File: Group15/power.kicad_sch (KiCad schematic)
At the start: 4 parts, among them J1 USB_C_Receptacle_USB2.0_16P, U3 AP63205WU

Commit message: corrected Power
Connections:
- net GND: no longer J1.A4 (VBUS), J1.A6 (D+), J1.A7 (D-), J1.A9 (VBUS), J1.B4 (VBUS), J1.B6 (D+), J1.B7 (D-), J1.B9 (VBUS)
- new net USB_D+: J1.A6 (D+), J1.B6 (D+)
- new net USB_D-: J1.A7 (D-), J1.B7 (D-)
- new net VBUS: J1.A4 (VBUS), J1.A9 (VBUS), J1.B4 (VBUS), J1.B9 (VBUS)
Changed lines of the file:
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@@
 	(paper "A4")
 	(junction
-		(at 67.31 113.03)
-		(diameter 0)
-		(color 0 0 0 0)
-	)
-	(junction
 		(at 59.69 85.09)
 		(diameter 0)
@@
 	)
 	(junction
-		(at 74.93 85.09)
-		(diameter 0)
-		(color 0 0 0 0)
-	)
-	(junction
-		(at 67.31 90.17)
-		(diameter 0)
-		(color 0 0 0 0)
-	)
-	(junction
 		(at 39.37 113.03)
 		(diameter 0)
@@
 	)
 	(junction
-		(at 55.88 113.03)
-		(diameter 0)
-		(color 0 0 0 0)
-	)
-	(junction
 		(at 63.5 71.12)
 		(diameter 0)
@@
 	)
 	(junction
-		(at 74.93 113.03)
-		(diameter 0)
-		(color 0 0 0 0)
-	)
-	(junction
 		(at 46.99 113.03)
 		(diameter 0)
@@
 	(junction
 		(at 59.69 90.17)
-		(diameter 0)
-		(color 0 0 0 0)
-	)
-	(junction
-		(at 88.9 71.12)
 		(diameter 0)
 		(color 0 0 0 0)
@@
 	(wire
 		(pts
-			(xy 63.5 71.12) (xy 88.9 71.12)
-		)
-		(stroke
-			(width 0)
-			(type default)
-		)
-	)
-	(wire
-		(pts
 			(xy 46.99 113.03) (xy 39.37 113.03)
 		)
@@
 	(wire
 		(pts
-			(xy 74.93 85.09) (xy 91.44 85.09)
-		)
-		(stroke
-			(width 0)
-			(type default)
-		)
-	)
-	(wire
-		(pts
-			(xy 88.9 71.12) (xy 91.44 71.12)
+			(xy 59.69 85.09) (xy 91.44 85.09)
+		)
+		(stroke
+			(width 0)
+			(type default)
+		)
+	)
+	(wire
+		(pts
+			(xy 63.5 71.12) (xy 91.44 71.12)
 		)
 		(stroke
@@
 	(wire
 		(pts
-			(xy 67.31 113.03) (xy 67.31 90.17)
-		)
-		(stroke
-			(width 0)
-			(type default)
-		)
-	)
-	(wire
-		(pts
 			(xy 59.69 83.82) (xy 59.69 85.09)
 		)
@@
 	(wire
 		(pts
-			(xy 74.93 113.03) (xy 74.93 85.09)
-		)
-		(stroke
-			(width 0)
-			(type default)
-		)
-	)
-	(wire
-		(pts
 			(xy 59.69 86.36) (xy 54.61 86.36)
 		)
@@
 	(wire
 		(pts
-			(xy 91.44 90.17) (xy 67.31 90.17)
-		)
-		(stroke
-			(width 0)
-			(type default)
-		)
-	)
-	(wire
-		(pts
 			(xy 59.69 88.9) (xy 59.69 90.17)
 		)
@@
 	(wire
 		(pts
-			(xy 67.31 90.17) (xy 59.69 90.17)
+			(xy 59.69 90.17) (xy 91.44 90.17)
 		)
 		(stroke
@@
 		)
 		(stroke
-			(width 0)
-			(type default)
-		)
-	)
-	(wire
-		(pts
-			(xy 59.69 85.09) (xy 74.93 85.09)
-		)
-		(stroke
-			(width 0)
-			(type default)
-		)
-	)
-	(wire
-		(pts
-			(xy 55.88 113.03) (xy 88.9 113.03)
-		)
-		(stroke
-			(width 0)
-			(type default)
-		)
-	)
-	(wire
-		(pts
-			(xy 88.9 113.03) (xy 88.9 71.12)
-		)
-		(stroke

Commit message: ADC
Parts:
- added C4, C5: 100 nF, symbol Device:C_Small
- added C6: 10 uF, symbol Device:C_Small
- added DAC1: (no value), symbol Symbol_Library:MCP4716A0T-E/CH
- added R8, R9: 5k6, symbol Device:R
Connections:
- net GND: now also C4.2, C5.2, C6.2, DAC1.2 (Vss)
- new net: DAC1.4 (SDA), R9.2
- new net: DAC1.5 (SCL), R8.2
- new net +3.3V: C4.1, C6.1, DAC1.3 (VDD), R8.1, R9.1
- new net DAC_OUT: C5.1, DAC1.1 (Vout)
- no-connect marks 2 -> 3

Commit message: added Footprint for DAC
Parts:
- DAC1: footprint (none) -> Package_TO_SOT_SMD:SOT-23-6
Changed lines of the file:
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@@
 			)
 		)
-		(property "Footprint" ""
+		(property "Footprint" "Package_TO_SOT_SMD:SOT-23-6"
 			(at 212.09 87.63 0)
 			(hide yes)

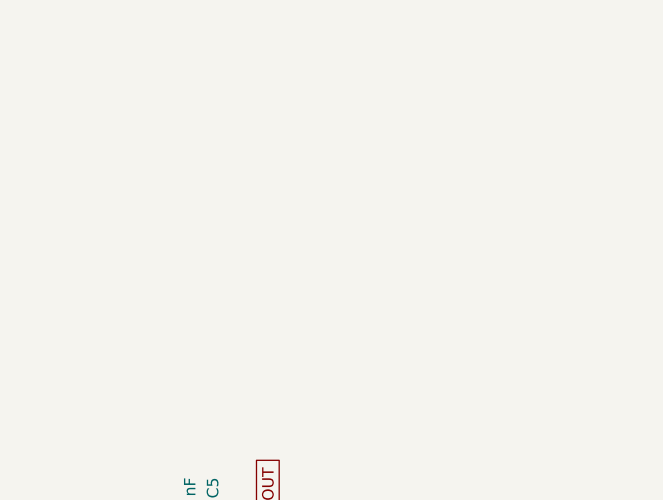
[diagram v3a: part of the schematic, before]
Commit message: changes in LDO
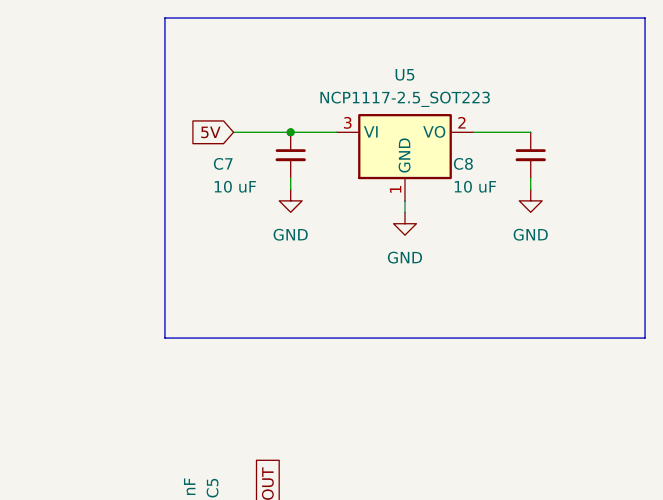
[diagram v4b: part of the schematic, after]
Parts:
- added C7, C8: 10 uF, symbol Device:C_Small
- added U5: NCP1117-2.5_SOT223, Package_TO_SOT_SMD:SOT-223-3_TabPin2, symbol Regulator_Linear:NCP1117-2.5_SOT223
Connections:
- net GND: now also C7.2, C8.2, U5.1 (GND)
- new net: C8.1, U5.2 (VO)
- new net 5V: C7.1, U5.3 (VI)

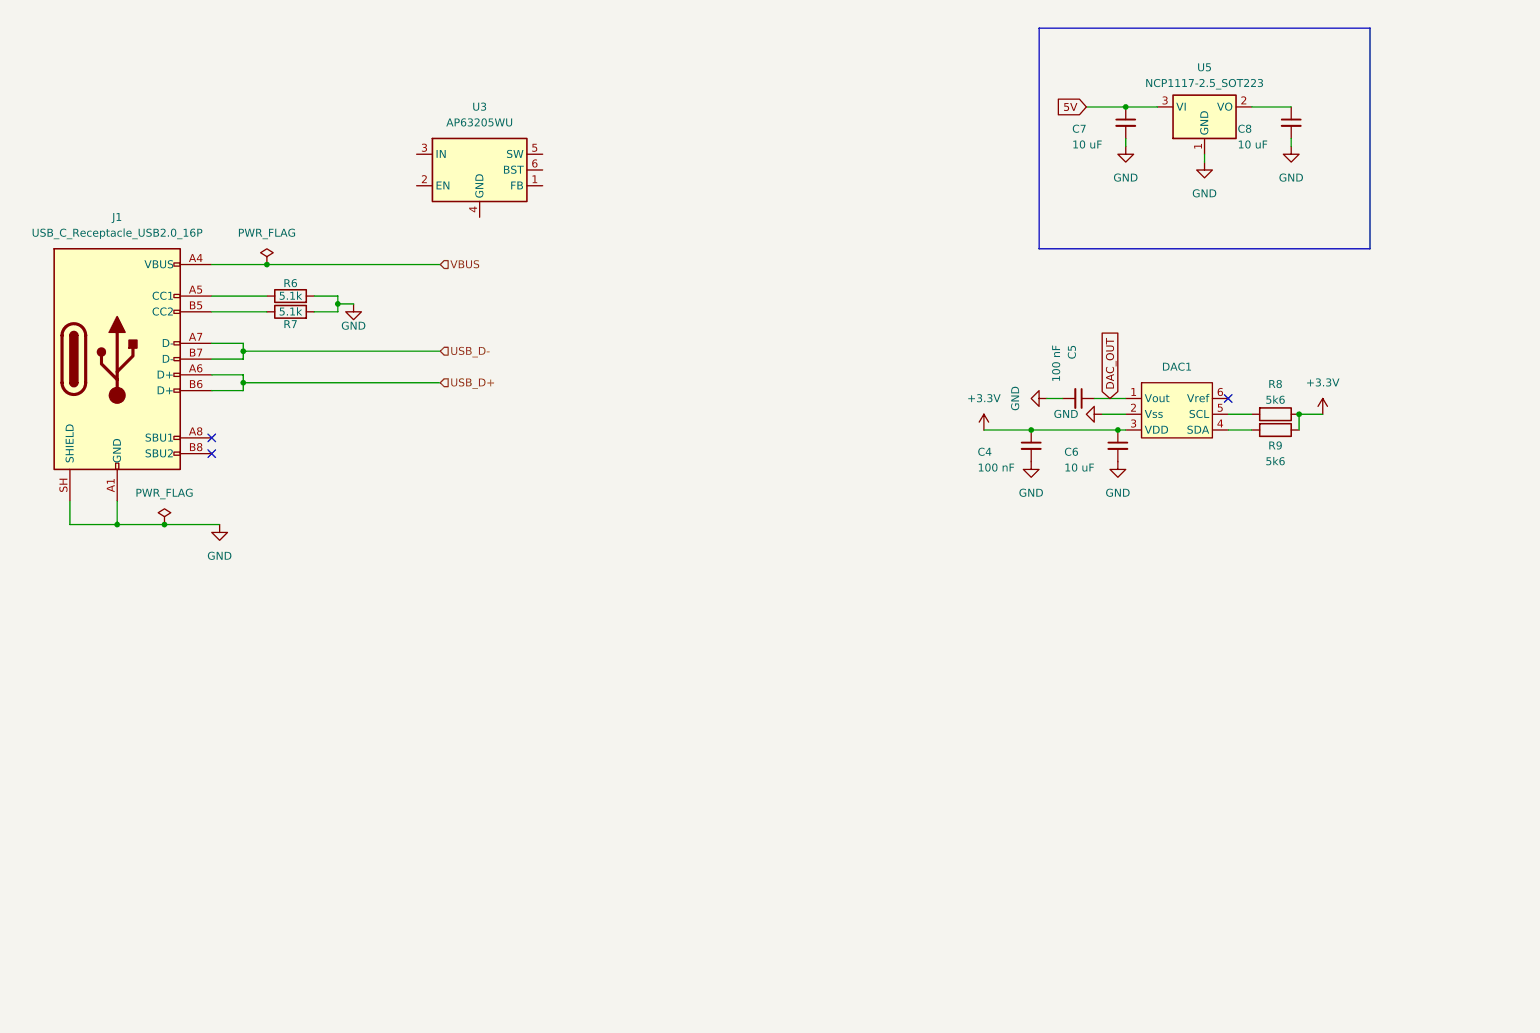
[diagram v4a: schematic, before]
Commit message: changes in Buck
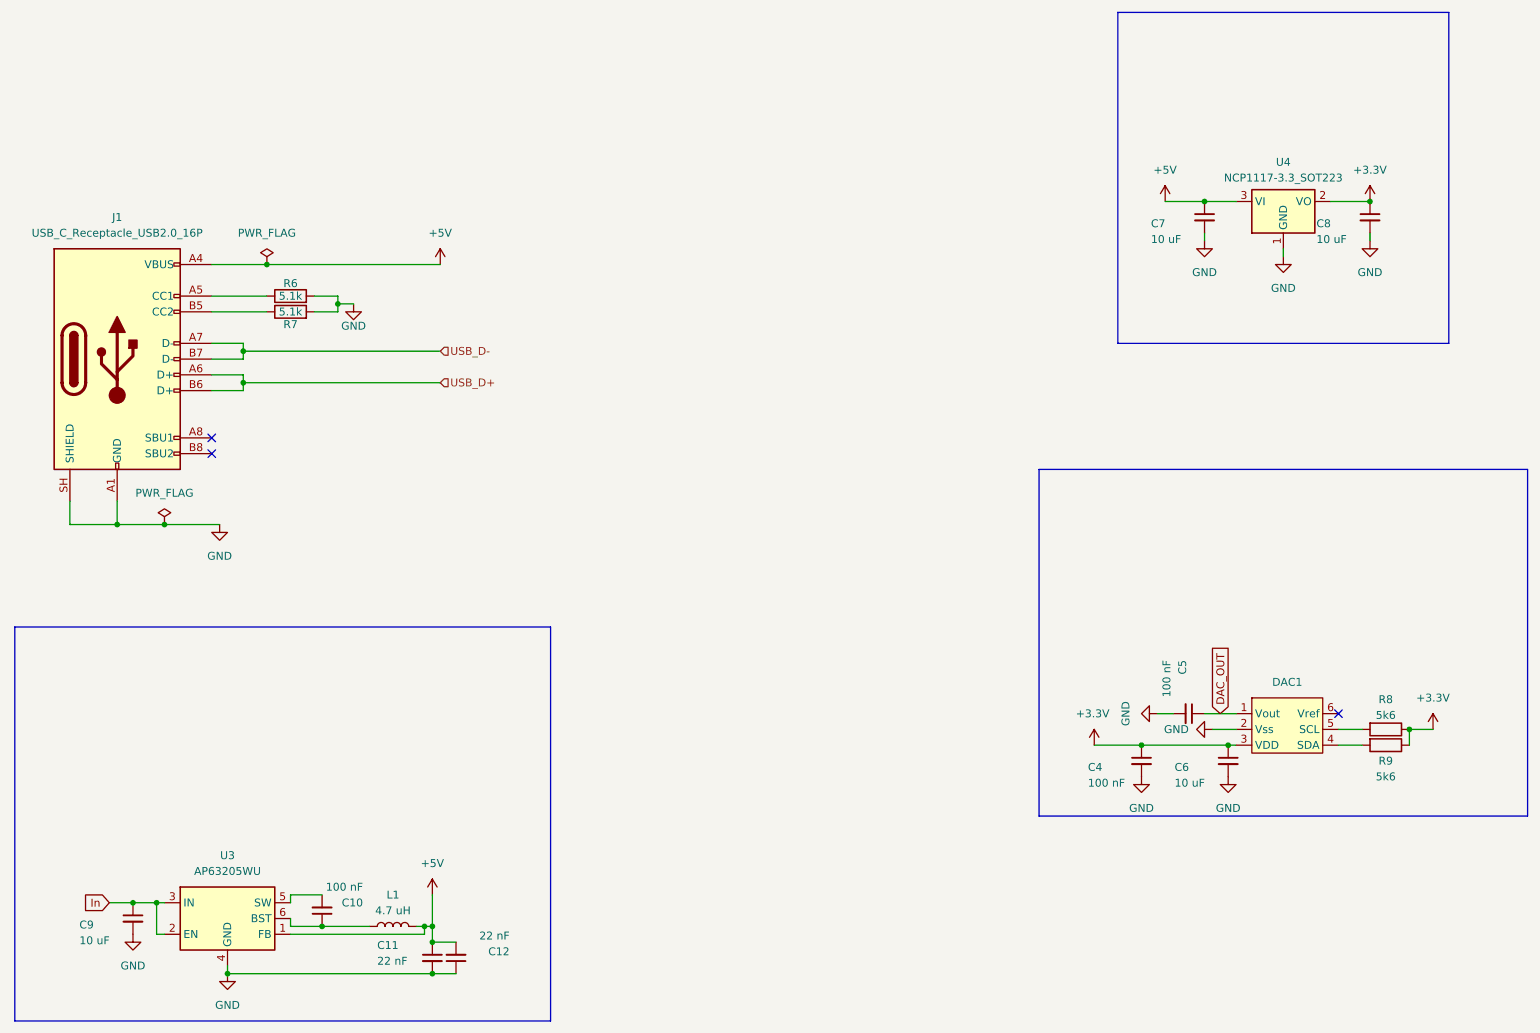
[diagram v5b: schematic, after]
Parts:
- removed U5: NCP1117-2.5_SOT223, Package_TO_SOT_SMD:SOT-223-3_TabPin2, symbol Regulator_Linear:NCP1117-2.5_SOT223
- added C10: 100 nF, symbol Device:C_Small
- added C11, C12: 22 nF, symbol Device:C_Small
- added C9: 10 uF, symbol Device:C_Small
- added L1: 4.7 uH, symbol Device:L
- added U4: NCP1117-3.3_SOT223, Package_TO_SOT_SMD:SOT-223-3_TabPin2, symbol Regulator_Linear:NCP1117-3.3_SOT223
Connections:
- net 5V is gone; now on net +5V: C7.1
- net VBUS is gone; now on net +5V: J1.A4 (VBUS), J1.A9 (VBUS), J1.B4 (VBUS), J1.B9 (VBUS)
- net +3.3V: now also C8.1, U4.2 (VO)
- net GND: now also U3.4 (GND), C11.2, C12.1, C9.2, U4.1 (GND)
- net +5V: now reaches U3.1 (FB)
- net +5V: now also C11.1, C12.2, L1.2, U4.3 (VI)
- net In: now reaches U3.2 (EN)
- net In: now also U3.3 (IN), C9.1
- net at U3.5 (SW): now also C10.2
- net at U3.6 (BST): now also C10.1, L1.1
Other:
- moved on the sheet: C4, C5, C6, C7, C8, DAC1, R8, R9, U3

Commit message: changes in Temp
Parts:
- added C13: 100 nF, symbol Device:C_Small
- added NTC_1: 10k, Resistor_SMD:R_0805_2012Metric, symbol Device:R
- added R10+-1%: 10k, symbol Device:R
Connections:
- net +3.3V: now also R10+-1%.2
- net GND: now also C13.2, NTC_1.1
- new net ADC1_uc: C13.1, NTC_1.2, R10+-1%.1
